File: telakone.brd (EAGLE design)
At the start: 100 x 100 mm, 156 parts, among them X11 MPT0.5/8-2.54, X2 MPT0.5/8-2.54, X3 MPT0.5/8-2.54, X4 PIIKKIRIMA-2, X5 PIIKKIRIMA-5, X7 U.FL-R-SMT-1, X8 MPT0.5/8-2.54, X9 629105136821

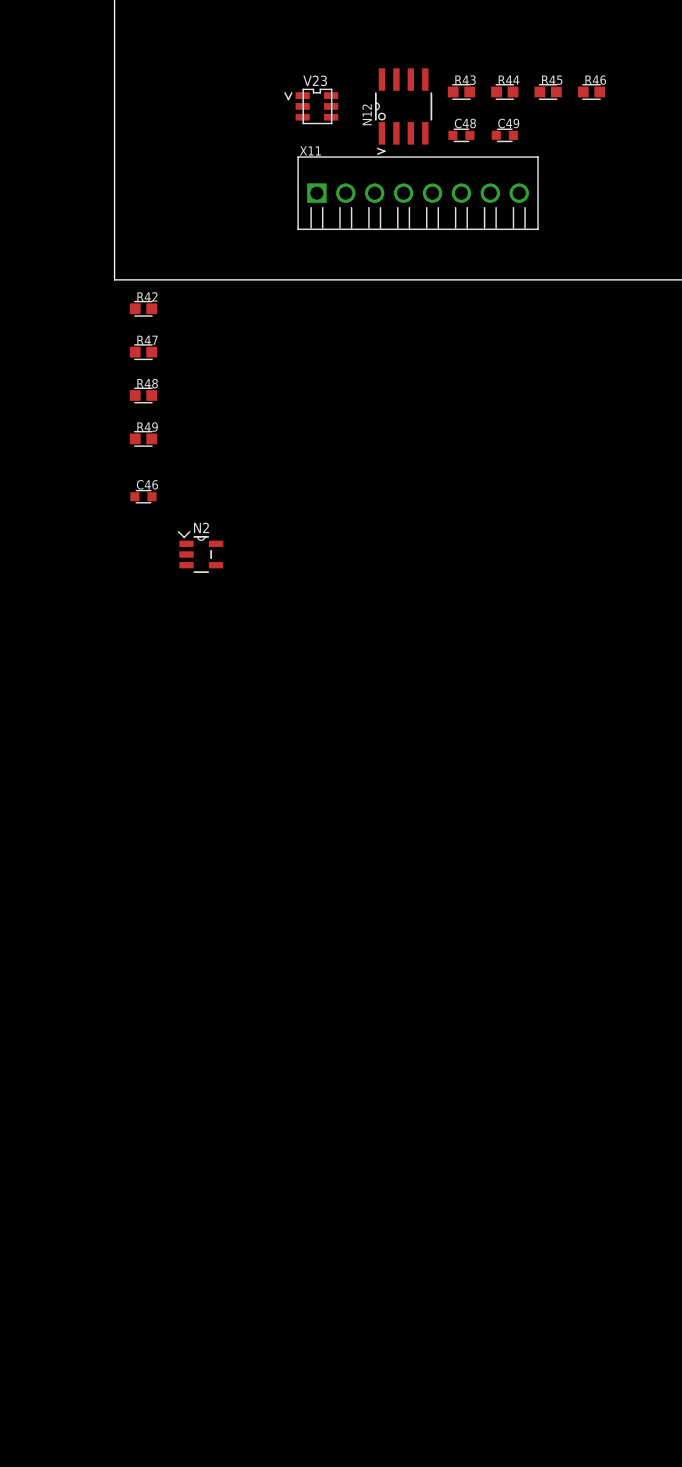
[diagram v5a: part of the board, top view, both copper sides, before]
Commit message: speed sensor inputs
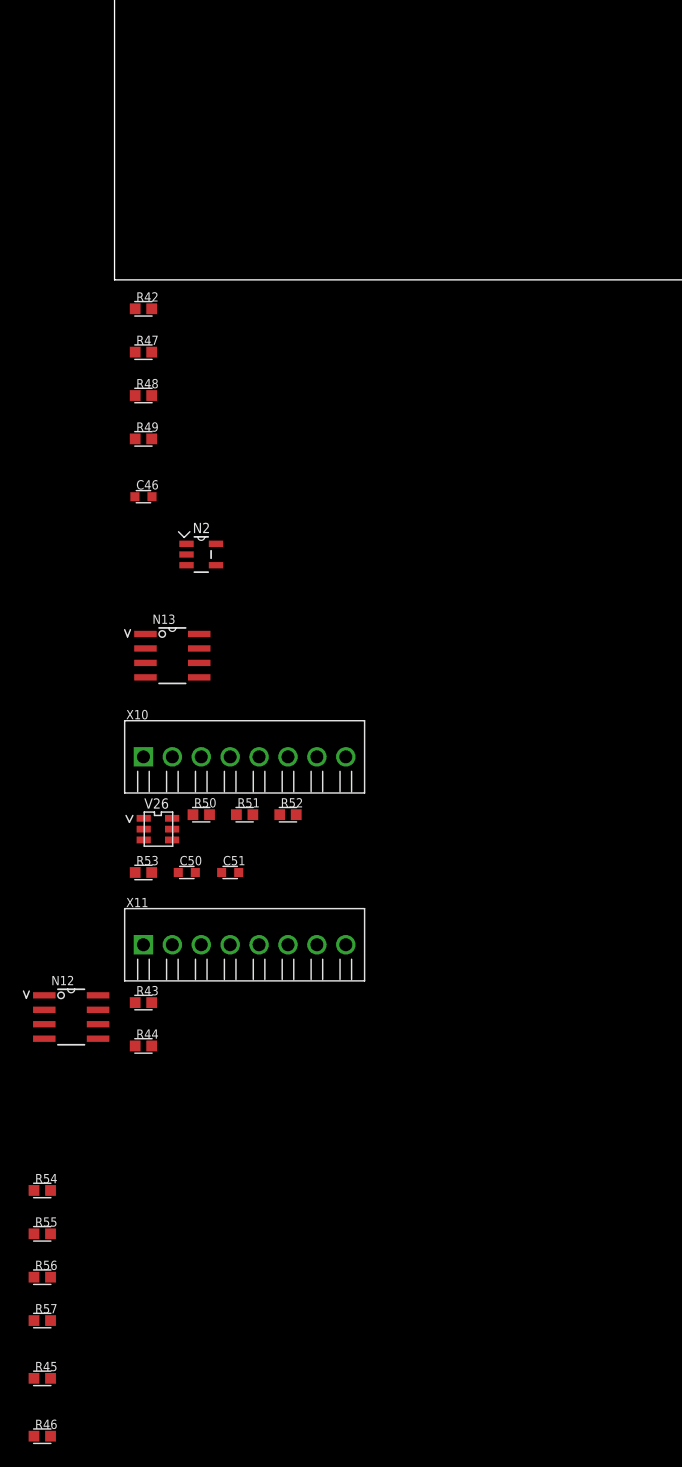
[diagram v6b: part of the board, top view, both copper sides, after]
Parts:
- removed C48, C49: (no value), omat_ic_2:C0603
- removed V23: WURTH 82402304, omat_ic_2:SOT23-6
- added C50, C51: (no value), omat_ic_2:C0603
- added N13: TS921IDT, omat_ic_2:SOIC8-N_MC
- added R50, R51: (no value), omat_ic_2:R0603
- added R52, R53: 2k00, omat_ic_2:R0603
- added R54, R55: 30k1, omat_ic_2:R0603
- added R56, R57: 5k90, omat_ic_2:R0603
- added V26: WURTH 82402304, omat_ic_2:SOT23-6
- added X10: MPT0.5/8-2.54, omat_ic_2:MPT0.5/8-2.54
- N12: value TS921IDT -> AZV3002S
- R28, R29, R46: value (none) -> 2k00
- R43, R44: value (none) -> 1k
- R45: value (none) -> 499
- moved R46 127.6 mm to (-6.35, -101.6)
- moved R45 121.5 mm to (-6.35, -96.5)
- moved R44 89.6 mm to (2.54, -67.3)
- moved N12 85.2 mm to (-3.81, -64.8), turned to 0 degrees
- moved R43 84.7 mm to (2.54, -63.5)
- moved X11 67.8 mm to (2.54, -58.4)
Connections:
- new net N$25: R50.2, X10.4
- new net N$43: R51.2, X10.7
- new net SPEED1: D1.81, N12.1
- new net SPEED2: D1.82, N12.7
- new net SPEED_SENSOR_1: R43.1, R54.2, X11.2
- new net SPEED_SENSOR_2: R44.1, R55.2, X11.5
- new net VREF25BUF: N13.2, N13.6, R46.2, X10.3, X10.6
- net +12V: now also R43.2, R44.2, X11.1, X11.4
- net +3V3: now also N12.8, N13.7, R52.2, R53.2; no longer N12.7, R45.2, R46.2
- net BUTTON1: now also R52.1, V26.1, X10.1; no longer R45.1, V23.1, X11.1
- net BUTTON2: now also R53.1, V26.3, X10.2; no longer R46.1, V23.3, X11.2
- net GND: now also C50.2, C51.2, N13.4, R45.1, R56.1, R57.1, V26.2, V26.5, X10.5, X10.8, X11.3, X11.6; no longer C48.2, C49.2, V23.2, V23.5, X11.5
- net N$12: now also N12.5, R55.1, R57.2; no longer R43.2, X11.4
- net N$14: now also N12.2, N12.6, R45.2, R46.1; no longer R44.2, X11.7
- net N$5: now also N12.3, R54.1, R56.2; no longer N12.2, N12.6, X11.3, X11.6
- net POT1: now also C51.1, R50.1, V26.4; no longer C49.1, R43.1, V23.4
- net POT2: now also C50.1, R51.1, V26.6; no longer C48.1, R44.1, V23.6
- net VREF25: now also N13.3; no longer N12.3

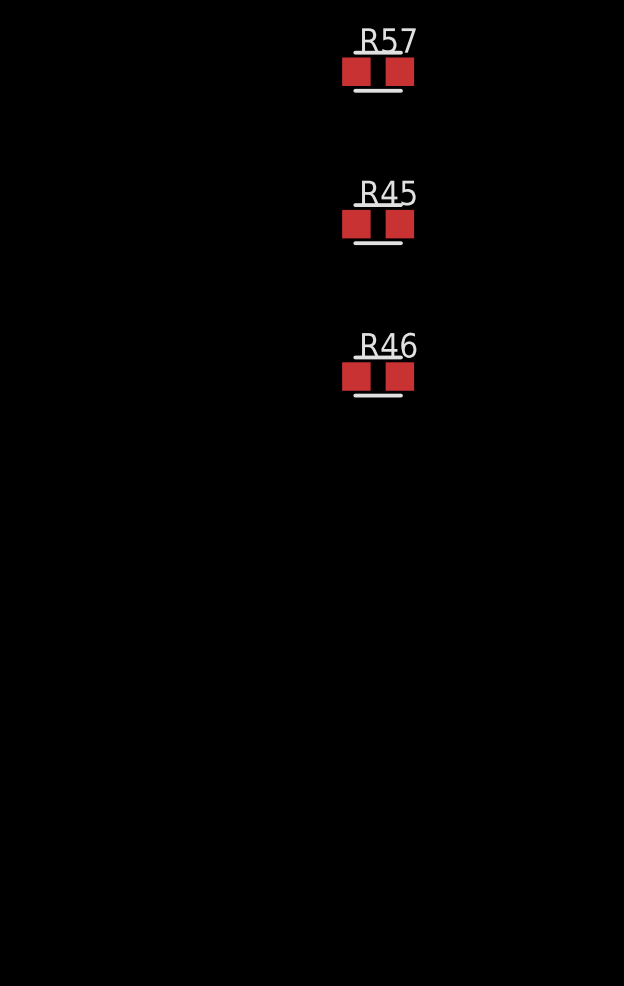
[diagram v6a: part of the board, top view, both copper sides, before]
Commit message: add accessory link 485 transceiver
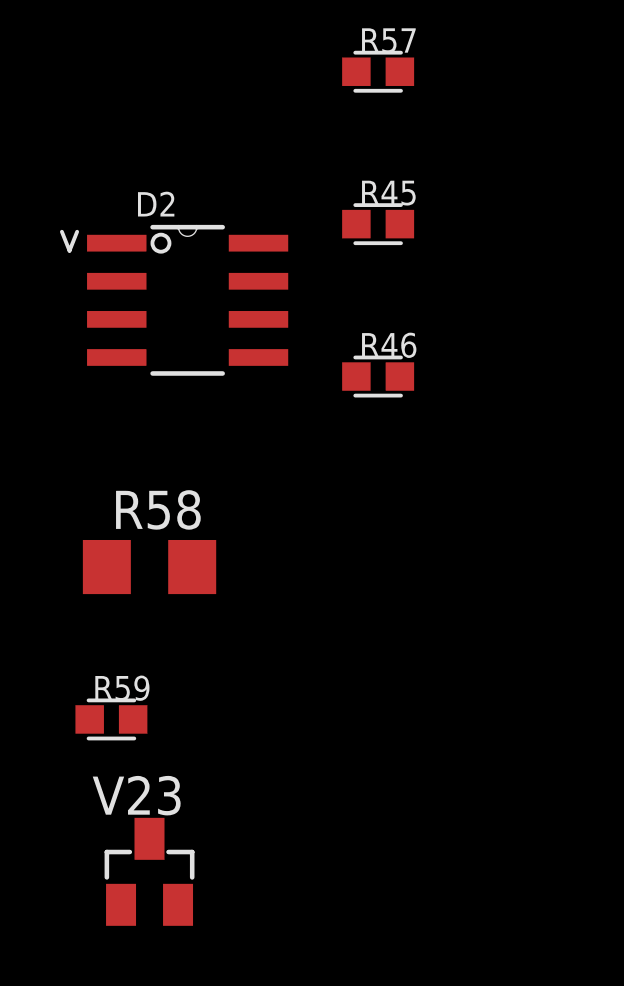
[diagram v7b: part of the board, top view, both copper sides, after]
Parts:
- added D2: MAX3430_SA, omat_ic_2:SOIC8-N_MC
- added R58: 121, omat_ic_2:R1206
- added R59: (no value), omat_ic_2:R0603
- added V23: SM712, omat_ic_2:SOT23
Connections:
- new net ACCLINKRX: D1.122, D2.1
- new net ACCLINKTX: D1.119, D2.4
- new net ACCLINKTXE: D1.118, D2.2, D2.3, R59.2
- new net ACCRTXHI: D2.6, R58.2, V23.1, X11.7
- new net ACCRTXLO: D2.7, R58.1, V23.2, X11.8
- net +3V3: now also D2.8
- net GND: now also D2.5, R59.1, V23.3; no longer X11.8
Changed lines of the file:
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@@
 <element name="R45" library="omat_ic_2" package="R0603" value="499" x="-6.35" y="-96.52"/>
 <element name="R46" library="omat_ic_2" package="R0603" value="2k00" x="-6.35" y="-101.6"/>
+<element name="D2" library="omat_ic_2" package="SOIC8-N_MC" value="MAX3430_SA" x="-12.7" y="-99.06"/>
+<element name="R58" library="omat_ic_2" package="R1206" value="121" x="-13.97" y="-107.95"/>
+<element name="R59" library="omat_ic_2" package="R0603" value="" x="-15.24" y="-113.03"/>
+<element name="V23" library="omat_ic_2" package="SOT23" value="SM712" x="-13.97" y="-118.11"/>
 </elements>
 <signals>
@@
 <contactref element="X11" pad="3"/>
 <contactref element="X11" pad="6"/>
-<contactref element="X11" pad="8"/>
 <contactref element="N12" pad="4"/>
 <contactref element="R56" pad="1"/>
 <contactref element="R57" pad="1"/>
 <contactref element="R45" pad="1"/>
+<contactref element="D2" pad="5"/>
+<contactref element="R59" pad="1"/>
+<contactref element="V23" pad="3"/>
 <wire x1="151.53" y1="81.915" x2="151.53" y2="88.265" width="0" layer="19" extent="1-1"/>
 <wire x1="154.21" y1="77.47" x2="151.53" y2="81.915" width="0" layer="19" extent="1-1"/>
@@
 <wire x1="7.62" y1="-58.42" x2="7.1" y2="-52.07" width="0" layer="19" extent="1-1"/>
 <wire x1="15.24" y1="-58.42" x2="7.62" y2="-58.42" width="0" layer="19" extent="1-1"/>
-<wire x1="20.32" y1="-58.42" x2="15.24" y2="-58.42" width="0" layer="19" extent="1-1"/>
 <wire x1="-6.1722" y1="-66.675" x2="7.62" y2="-58.42" width="0" layer="19" extent="1-1"/>
 <wire x1="-7.075" y1="-87.63" x2="-6.1722" y2="-66.675" width="0" layer="19" extent="1-1"/>
 <wire x1="-7.075" y1="-91.44" x2="-7.075" y2="-87.63" width="0" layer="19" extent="1-1"/>
 <wire x1="-7.075" y1="-96.52" x2="-7.075" y2="-91.44" width="0" layer="19" extent="1-1"/>
+<wire x1="-10.3378" y1="-100.965" x2="-7.075" y2="-96.52" width="0" layer="19" extent="1-1"/>
+<wire x1="-15.965" y1="-113.03" x2="-10.3378" y2="-100.965" width="0" layer="19" extent="1-1"/>
+<wire x1="-13.97" y1="-117.01" x2="-15.965" y2="-113.03" width="0" layer="19" extent="1-1"/>
 </signal>
 <signal name="N$4">
@@
 <contactref element="R53" pad="2"/>
 <contactref element="N12" pad="8"/>
+<contactref element="D2" pad="8"/>
 <wire x1="151.53" y1="80.645" x2="151.53" y2="84.455" width="0" layer="19" extent="1-1"/>
 <wire x1="151.53" y1="79.375" x2="151.53" y2="80.645" width="0" layer="19" extent="1-1"/>
@@
 <wire x1="3.265" y1="-52.07" x2="15.965" y2="-46.99" width="0" layer="19" extent="1-1"/>
 <wire x1="-1.4478" y1="-62.865" x2="3.265" y2="-52.07" width="0" layer="19" extent="1-1"/>
+<wire x1="-10.3378" y1="-97.155" x2="-1.4478" y2="-62.865" width="0" layer="19" extent="1-1"/>
 </signal>
 <signal name="THROTTLE_BUFFERED_1">
@@
 <wire x1="-6.1722" y1="-64.135" x2="-1.4478" y2="-65.405" width="0" layer="19" extent="1-1"/>
 </signal>
+<signal name="ACCRTXLO">
+<contactref element="D2" pad="7"/>
+<contactref element="R58" pad="1"/>
+<contactref element="X11" pad="8"/>
+<contactref element="V23" pad="2"/>
+<wire x1="-15.392" y1="-107.95" x2="-13.02" y2="-119.21" width="0" layer="19" extent="1-1"/>
+<wire x1="-10.3378" y1="-98.425" x2="-15.392" y2="-107.95" width="0" layer="19" extent="1-1"/>
+<wire x1="20.32" y1="-58.42" x2="-10.3378" y2="-98.425" width="0" layer="19" extent="1-1"/>
+</signal>
+<signal name="ACCRTXHI">
+<contactref element="D2" pad="6"/>
+<contactref element="R58" pad="2"/>
+<contactref element="X11" pad="7"/>
+<contactref element="V23" pad="1"/>
+<wire x1="-12.548" y1="-107.95" x2="-14.92" y2="-119.21" width="0" layer="19" extent="1-1"/>
+<wire x1="-10.3378" y1="-99.695" x2="-12.548" y2="-107.95" width="0" layer="19" extent="1-1"/>
+<wire x1="17.78" y1="-58.42" x2="-10.3378" y2="-99.695" width="0" layer="19" extent="1-1"/>
+</signal>
+<signal name="ACCLINKTXE">
+<contactref element="D2" pad="2"/>
+<contactref element="D2" pad="3"/>
+<contactref element="D1" pad="118"/>
+<contactref element="R59" pad="2"/>
+<wire x1="-15.0622" y1="-99.695" x2="-14.515" y2="-113.03" width="0" layer="19" extent="1-1"/>
+<wire x1="-15.0622" y1="-98.425" x2="-15.0622" y2="-99.695" width="0" layer="19" extent="1-1"/>
+<wire x1="74.49" y1="27.475" x2="-15.0622" y2="-98.425" width="0" layer="19" extent="1-1"/>
+</signal>
+<signal name="ACCLINKTX">
+<contactref element="D2" pad="4"/>
+<contactref element="D1" pad="119"/>
+<wire x1="74.99" y1="27.475" x2="-15.0622" y2="-100.965" width="0" layer="19" extent="1-1"/>
+</signal>
+<signal name="ACCLINKRX">
+<contactref element="D2" pad="1"/>
+<contactref element="D1" pad="122"/>
+<wire x1="76.49" y1="27.475" x2="-15.0622" y2="-97.155" width="0" layer="19" extent="1-1"/>
+</signal>
 </signals>

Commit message: tuning
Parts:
- added V27: ESDAXXSC6, omat_ic_2:SOT23-6
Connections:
- removed net N$25: R50.2, X10.4
- removed net N$43: R51.2, X10.7
- new net POT_IN_1: R50.2, V26.4, X10.4
- new net POT_IN_2: R51.2, V26.6, X10.7
- net GND: now also V27.2, V27.5
- net POT1: no longer V26.4
- net POT2: no longer V26.6
- net SPEED_SENSOR_1: now also V27.3
- net SPEED_SENSOR_2: now also V27.4
- net VREF25BUF: now also V27.1
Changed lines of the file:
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@@
 <element name="R59" library="omat_ic_2" package="R0603" value="" x="-15.24" y="-113.03"/>
 <element name="V23" library="omat_ic_2" package="SOT23" value="SM712" x="-13.97" y="-118.11"/>
+<element name="V27" library="omat_ic_2" package="SOT23-6" value="ESDAXXSC6" x="-13.97" y="-125.73"/>
 </elements>
 <signals>
@@
 <contactref element="C51" pad="2"/>
 <contactref element="C50" pad="2"/>
-<contactref element="V26" pad="2"/>
-<contactref element="V26" pad="5"/>
 <contactref element="X11" pad="3"/>
 <contactref element="X11" pad="6"/>
@@
 <contactref element="R59" pad="1"/>
 <contactref element="V23" pad="3"/>
+<contactref element="V26" pad="2"/>
+<contactref element="V26" pad="5"/>
+<contactref element="V27" pad="2"/>
+<contactref element="V27" pad="5"/>
 <wire x1="151.53" y1="81.915" x2="151.53" y2="88.265" width="0" layer="19" extent="1-1"/>
 <wire x1="154.21" y1="77.47" x2="151.53" y2="81.915" width="0" layer="19" extent="1-1"/>
@@
 <wire x1="-15.965" y1="-113.03" x2="-10.3378" y2="-100.965" width="0" layer="19" extent="1-1"/>
 <wire x1="-13.97" y1="-117.01" x2="-15.965" y2="-113.03" width="0" layer="19" extent="1-1"/>
+<wire x1="-15.22" y1="-125.73" x2="-13.97" y2="-117.01" width="0" layer="19" extent="1-1"/>
+<wire x1="-12.72" y1="-125.73" x2="-15.22" y2="-125.73" width="0" layer="19" extent="1-1"/>
 </signal>
 <signal name="N$4">
@@
 <contactref element="R51" pad="1"/>
 <contactref element="C50" pad="1"/>
-<contactref element="V26" pad="6"/>
 <wire x1="10.705" y1="-46.99" x2="89.365" y2="36.35" width="0" layer="19" extent="1-1"/>
-<wire x1="5.06" y1="-47.31" x2="10.705" y2="-46.99" width="0" layer="19" extent="1-1"/>
-<wire x1="5.6" y1="-52.07" x2="5.06" y2="-47.31" width="0" layer="19" extent="1-1"/>
+<wire x1="5.6" y1="-52.07" x2="10.705" y2="-46.99" width="0" layer="19" extent="1-1"/>
 </signal>
 <signal name="POT1">
@@
 <contactref element="R50" pad="1"/>
 <contactref element="C51" pad="1"/>
-<contactref element="V26" pad="4"/>
 <wire x1="6.895" y1="-46.99" x2="89.365" y2="35.85" width="0" layer="19" extent="1-1"/>
-<wire x1="5.06" y1="-49.21" x2="6.895" y2="-46.99" width="0" layer="19" extent="1-1"/>
-<wire x1="9.41" y1="-52.07" x2="5.06" y2="-49.21" width="0" layer="19" extent="1-1"/>
+<wire x1="9.41" y1="-52.07" x2="6.895" y2="-46.99" width="0" layer="19" extent="1-1"/>
 </signal>
 <signal name="BUTTON1">
@@
 <contactref element="X10" pad="6"/>
 <contactref element="R46" pad="2"/>
+<contactref element="V27" pad="1"/>
+<wire x1="-5.625" y1="-101.6" x2="-15.22" y2="-124.78" width="0" layer="19" extent="1-1"/>
 <wire x1="7.62" y1="-41.91" x2="-5.625" y2="-101.6" width="0" layer="19" extent="1-1"/>
 <wire x1="15.24" y1="-41.91" x2="7.62" y2="-41.91" width="0" layer="19" extent="1-1"/>
@@
 <wire x1="2.7178" y1="-32.385" x2="7.4422" y2="-33.655" width="0" layer="19" extent="1-1"/>
 </signal>
-<signal name="N$25">
+<signal name="POT_IN_1">
 <contactref element="R50" pad="2"/>
 <contactref element="X10" pad="4"/>
+<contactref element="V26" pad="4"/>
+<wire x1="8.345" y1="-46.99" x2="5.06" y2="-49.21" width="0" layer="19" extent="1-1"/>
 <wire x1="10.16" y1="-41.91" x2="8.345" y2="-46.99" width="0" layer="19" extent="1-1"/>
 </signal>
-<signal name="N$43">
+<signal name="POT_IN_2">
 <contactref element="R51" pad="2"/>
 <contactref element="X10" pad="7"/>
+<contactref element="V26" pad="6"/>
+<wire x1="12.155" y1="-46.99" x2="5.06" y2="-47.31" width="0" layer="19" extent="1-1"/>
 <wire x1="17.78" y1="-41.91" x2="12.155" y2="-46.99" width="0" layer="19" extent="1-1"/>
 </signal>
@@
 <contactref element="R43" pad="1"/>
 <contactref element="R54" pad="2"/>
+<contactref element="V27" pad="3"/>
+<wire x1="-5.625" y1="-80.01" x2="-15.22" y2="-126.68" width="0" layer="19" extent="1-1"/>
 <wire x1="1.815" y1="-63.5" x2="-5.625" y2="-80.01" width="0" layer="19" extent="1-1"/>
 <wire x1="5.08" y1="-58.42" x2="1.815" y2="-63.5" width="0" layer="19" extent="1-1"/>
@@
 <contactref element="R44" pad="1"/>
 <contactref element="R55" pad="2"/>
+<contactref element="V27" pad="4"/>
+<wire x1="-5.625" y1="-83.82" x2="-12.72" y2="-126.68" width="0" layer="19" extent="1-1"/>
 <wire x1="1.815" y1="-67.31" x2="-5.625" y2="-83.82" width="0" layer="19" extent="1-1"/>
 <wire x1="12.7" y1="-58.42" x2="1.815" y2="-67.31" width="0" layer="19" extent="1-1"/>
